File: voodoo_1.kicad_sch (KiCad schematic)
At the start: 43 parts, among them Q1 2N2222, Q2 2N2222, SW1 SW_3PDT, U1 LM308

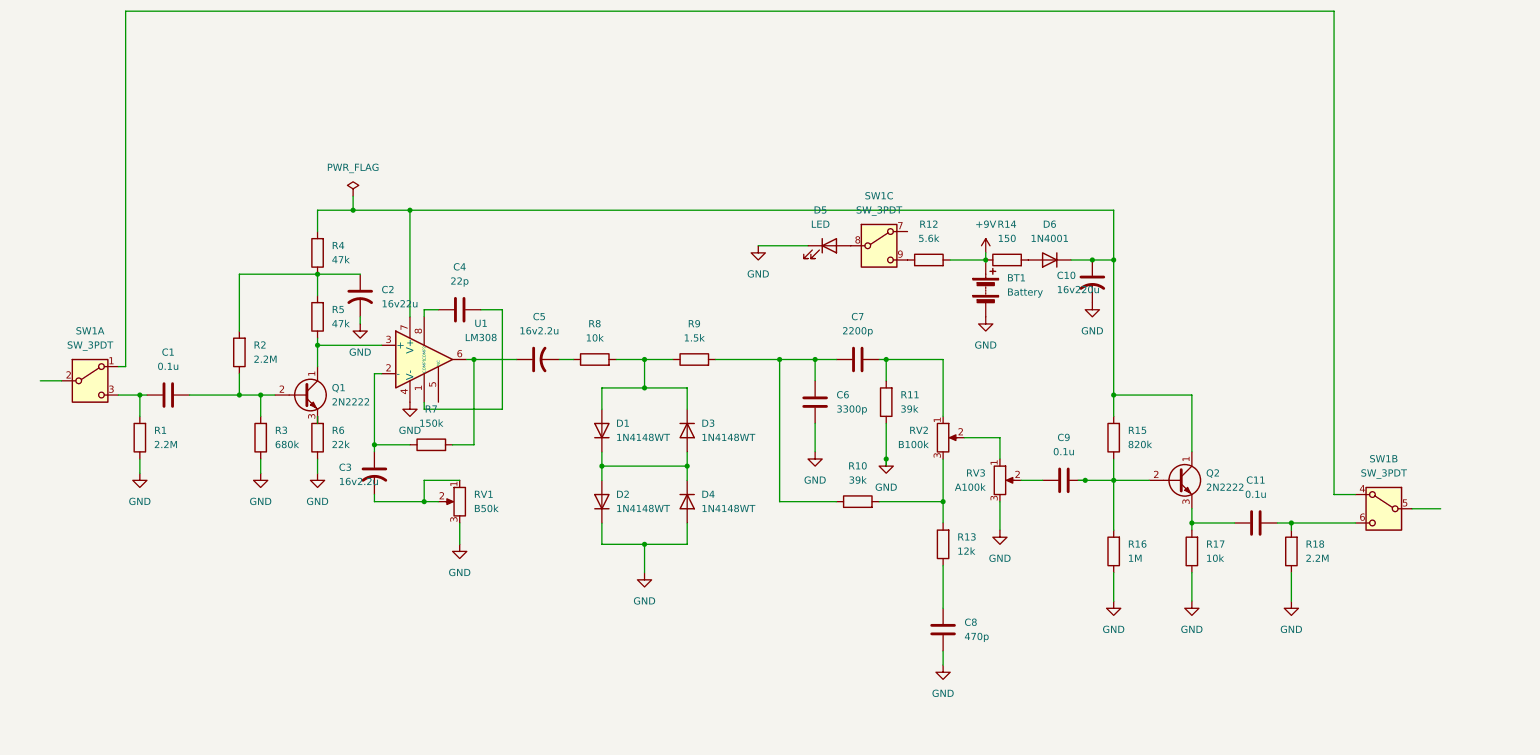
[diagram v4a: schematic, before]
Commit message: GNDを1.0mmに、ドリル穴を0.4mmに、部品の配置をやり直し。
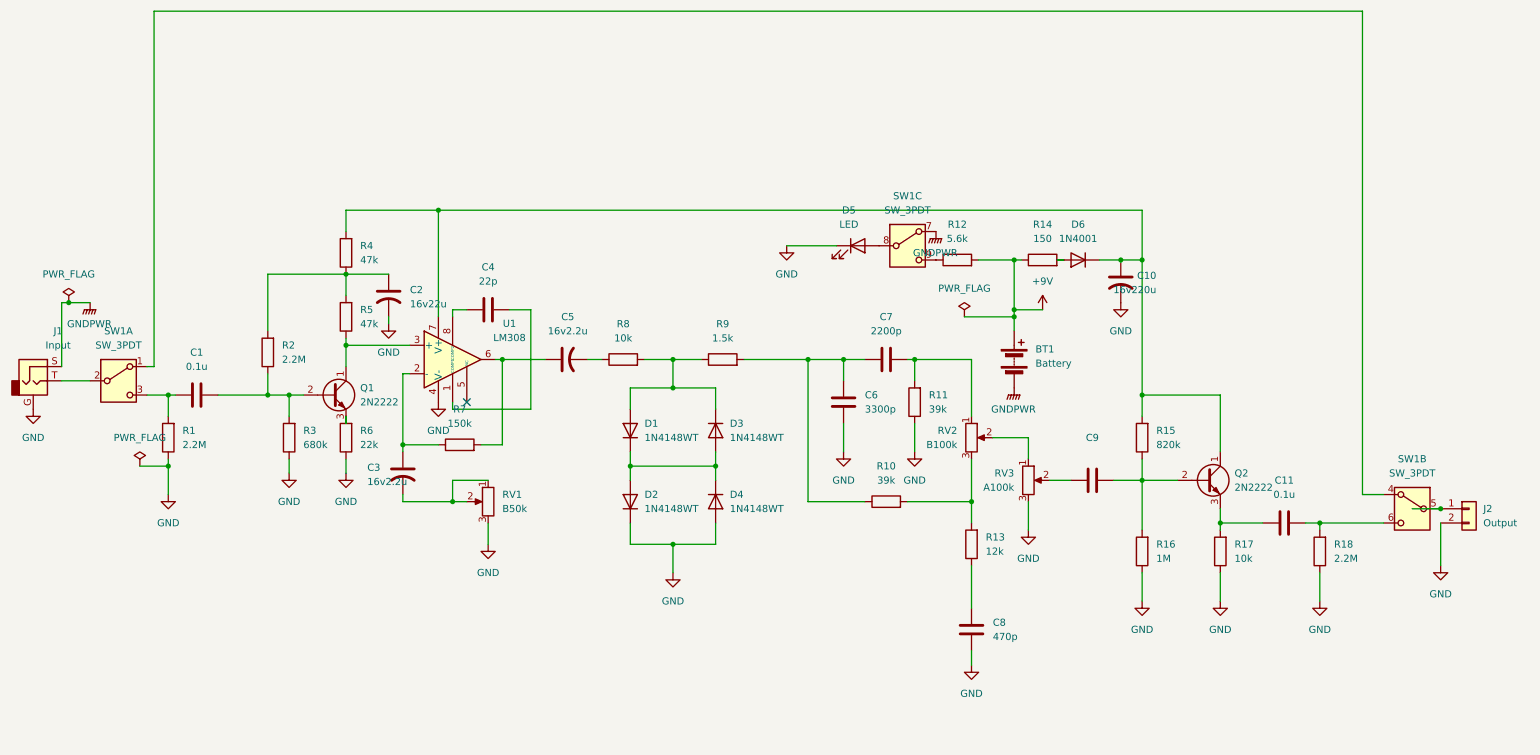
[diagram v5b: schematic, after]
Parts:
- added J1: Input, symbol Connector_Audio:AudioJack2_Ground
- added J2: Output, Connector_JST:JST_XH_B2B-XH-A_1x02_P2.50mm_Vertical, symbol Connector_Generic:Conn_01x02
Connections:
- net GND: now also J1.G, J2.2 (Pin_2); no longer BT1.2 (-)
- net at SW1.2 (B): now also J1.T
- net GNDPWR: now reaches SW1.7 (A)
- net GNDPWR: now also BT1.2 (-), J1.S
- net at SW1.5 (B): now also J2.1 (Pin_1)
- no-connect marks 0 -> 1
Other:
- moved on the sheet: BT1, C1, C10, C11, C2, C3, C4, C5, C6, C7, C8, C9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

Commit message: ネジ穴追加、配置修整、線は0.8mm、GNDは1.0mm。
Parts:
- added H1, H2, H3, H4: MountingHole, MountingHole:MountingHole_3.2mm_M3, symbol Mechanical:MountingHole
- J2: footprint Connector_JST:JST_XH_B2B-XH-A_1x02_P2.50mm_Vertical -> (none)

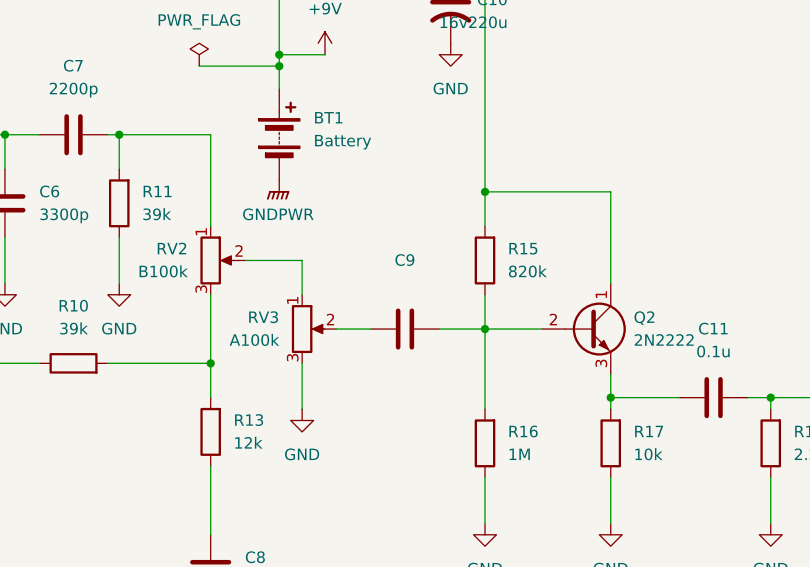
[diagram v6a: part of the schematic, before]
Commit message: 2n2222のピンアサイン修正、配置を詰めた。
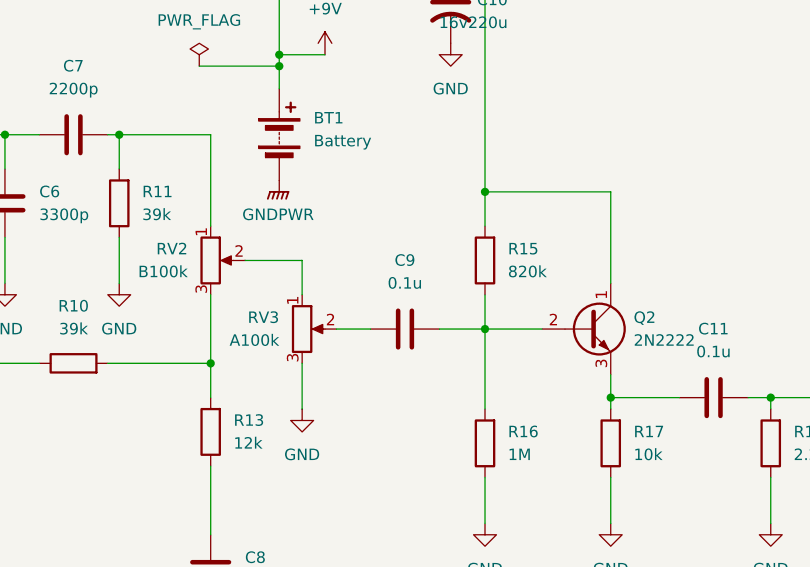
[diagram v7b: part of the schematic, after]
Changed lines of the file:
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@@
 					(size 1.27 1.27)
 				)
-				(hide yes)
 			)
 		)

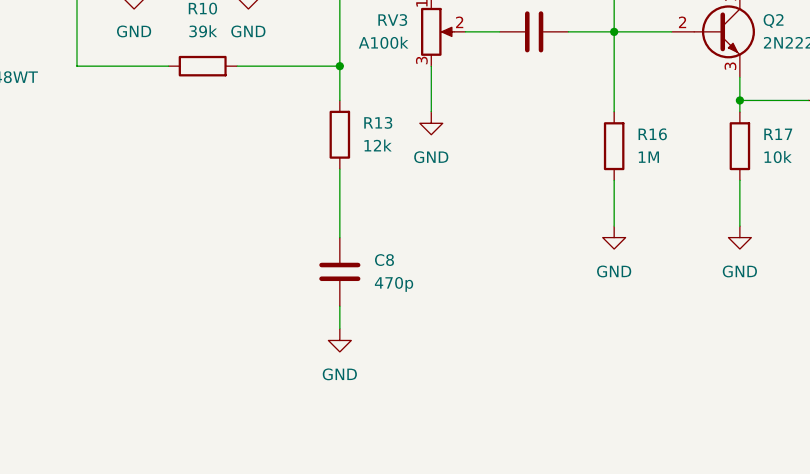
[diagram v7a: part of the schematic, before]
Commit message: C8のコンデンサ470pF -> 4700pF
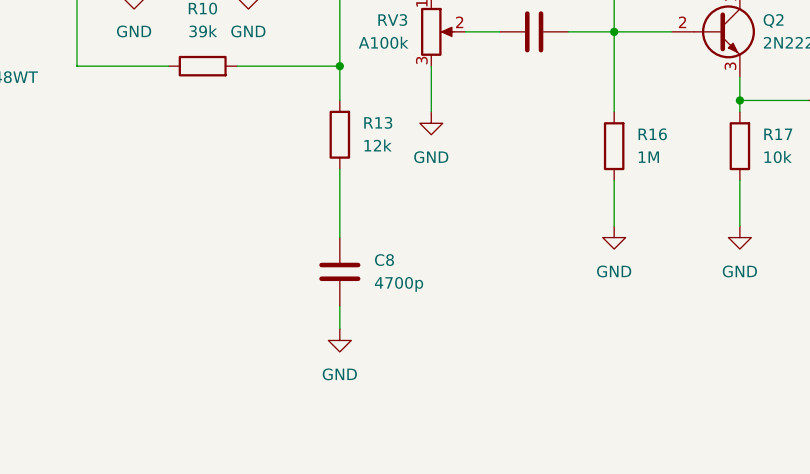
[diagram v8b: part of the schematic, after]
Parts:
- C8: value 470p -> 4700p
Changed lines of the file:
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@@
 			)
 		)
-		(property "Value" "470p"
+		(property "Value" "4700p"
 			(at 186.69 134.6199 0)
 			(effects
